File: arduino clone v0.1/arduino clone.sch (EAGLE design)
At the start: 18 parts, among them U101 ATMEGA328P_TQFP, U201 CH340G

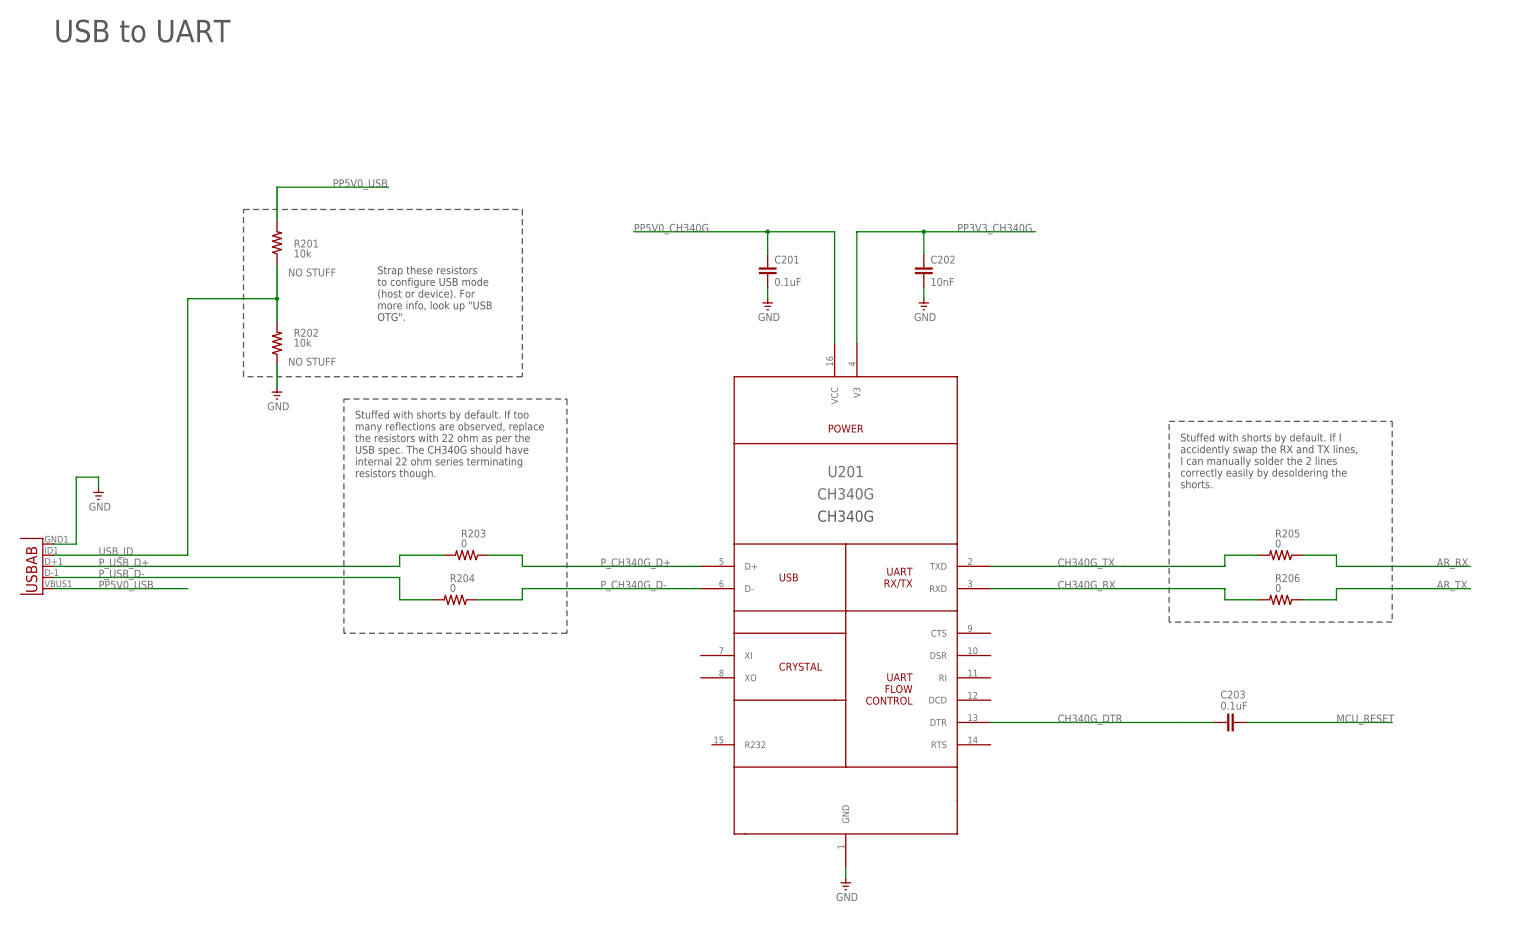
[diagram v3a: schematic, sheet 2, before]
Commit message: disconnect USB nets from connector
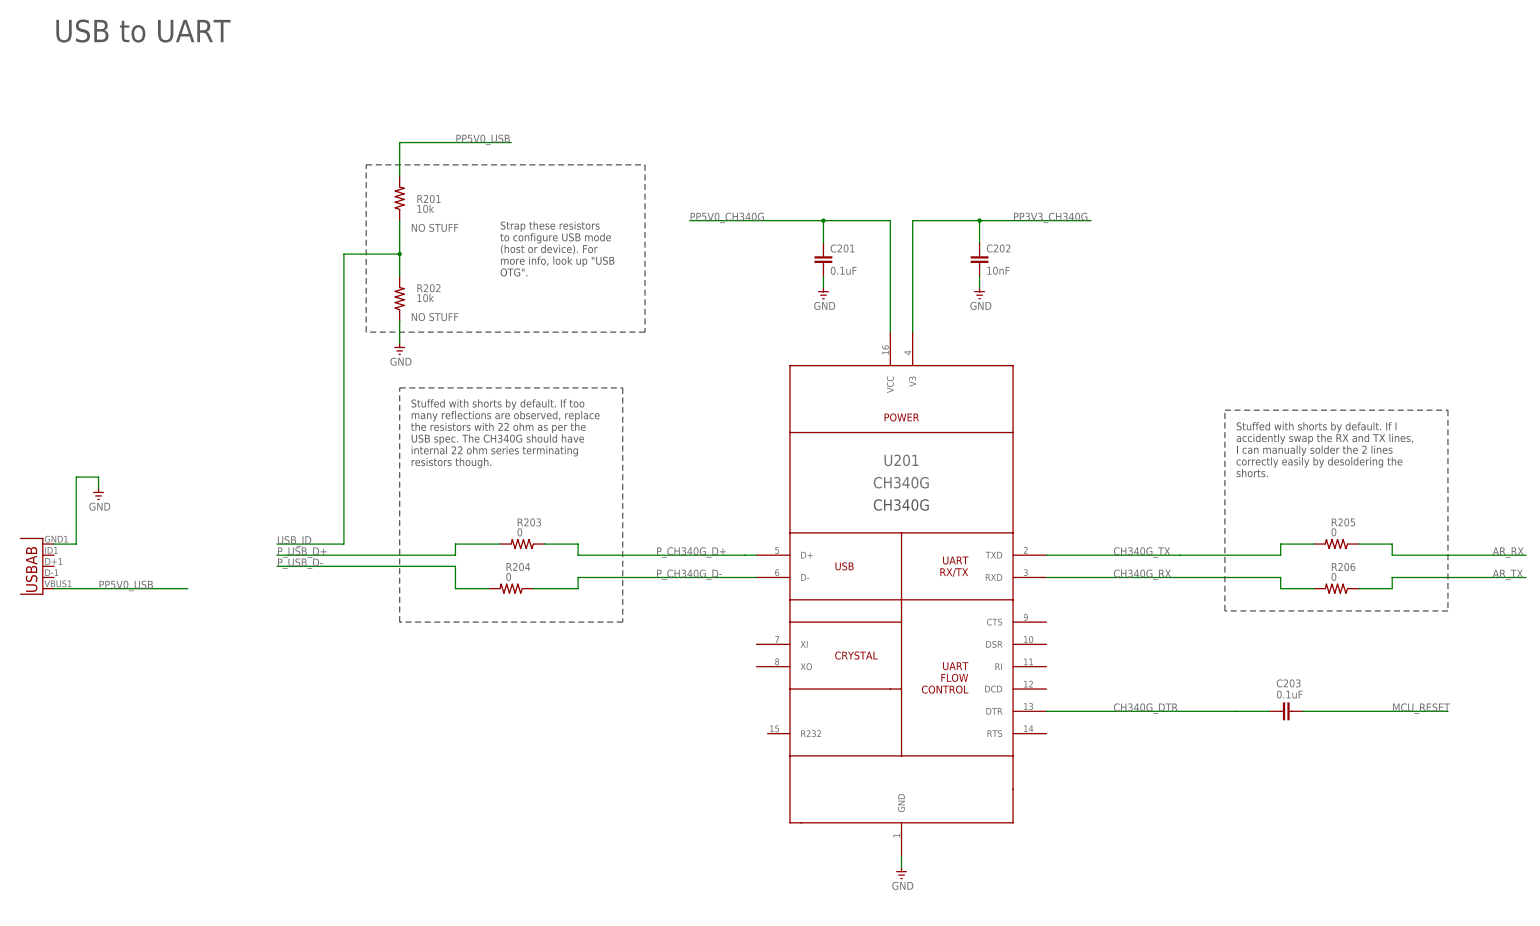
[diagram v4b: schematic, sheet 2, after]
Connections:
- net P_USB_D+: no longer J1.D+
- net P_USB_D-: no longer J1.D-
- net USB_ID: no longer J1.USBID
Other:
- moved on the sheet: C201, C202, C203, R201, R202, R203, R204, R205, R206, U201

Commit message: add signal nets to USB connector
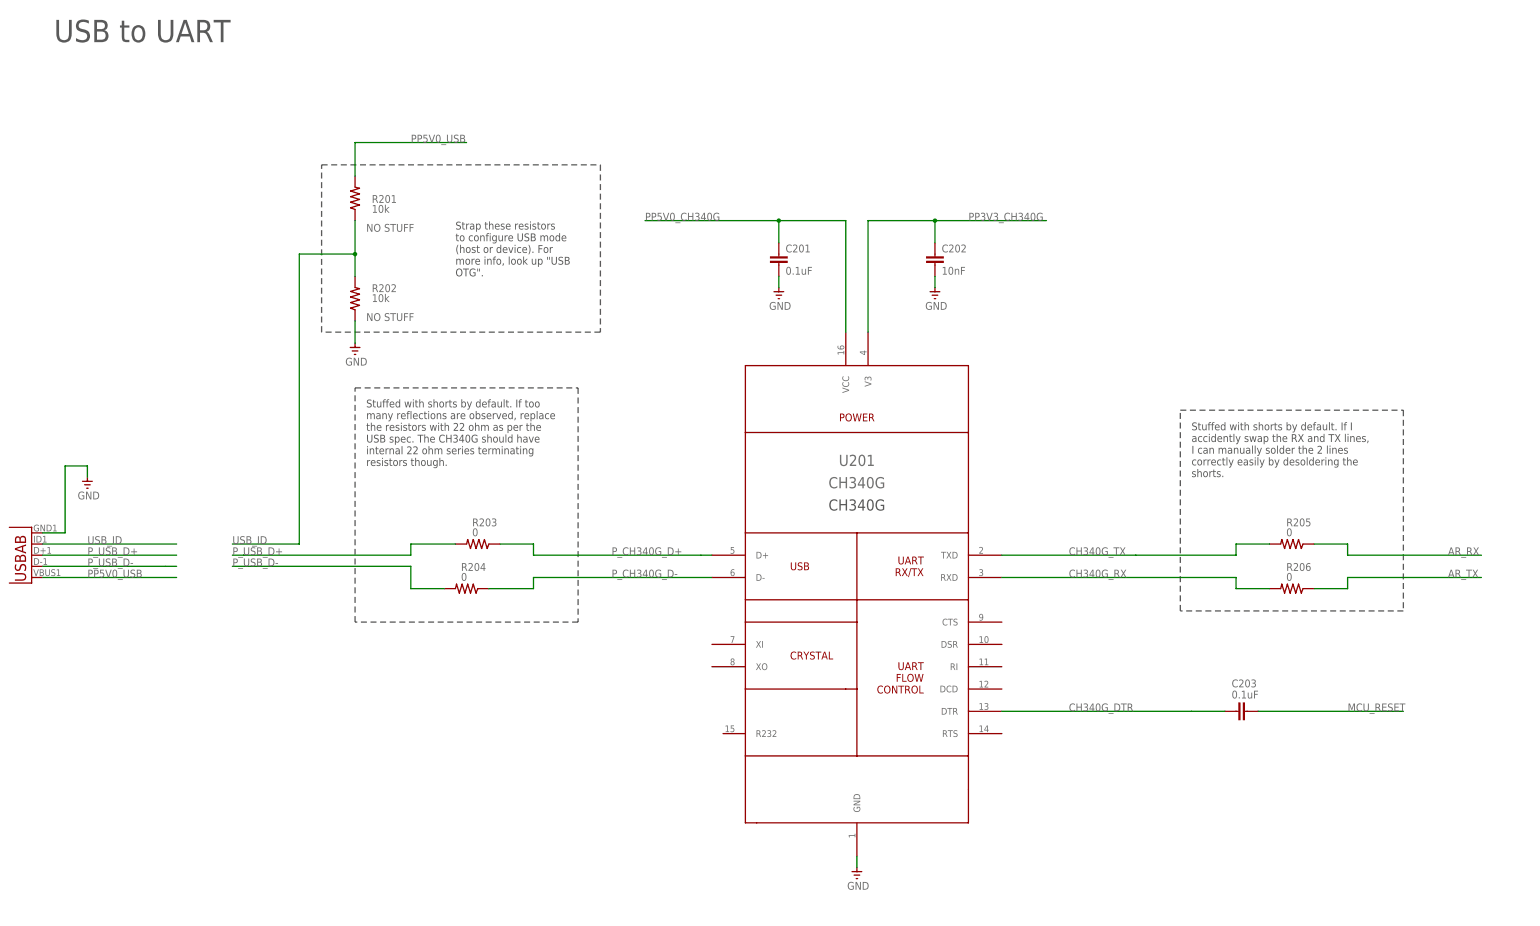
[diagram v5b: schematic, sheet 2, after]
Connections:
- net P_USB_D+: now also J1.D+
- net P_USB_D-: now also J1.D-
- net USB_ID: now also J1.USBID
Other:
- moved on the sheet: C201, C202, C203, R201, R202, R203, R204, R205, R206, U201

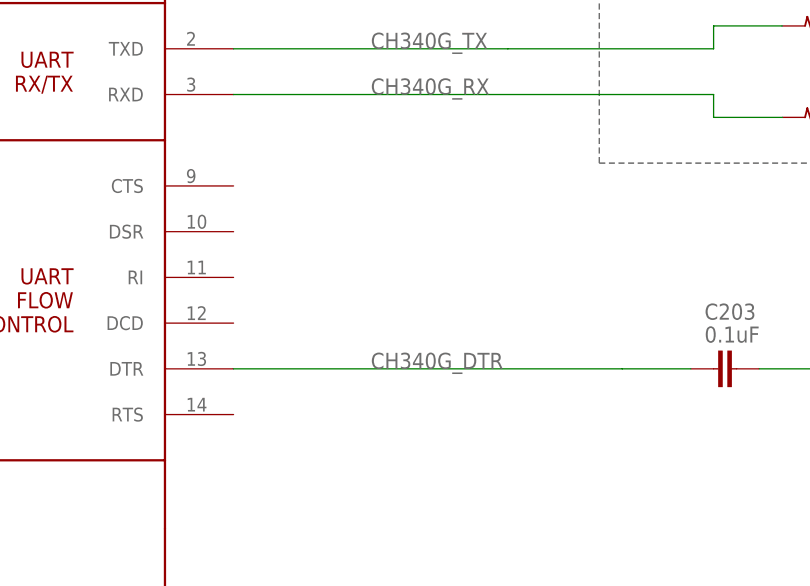
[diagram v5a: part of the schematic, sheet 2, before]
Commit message: add named nets for CH350G UART flow control
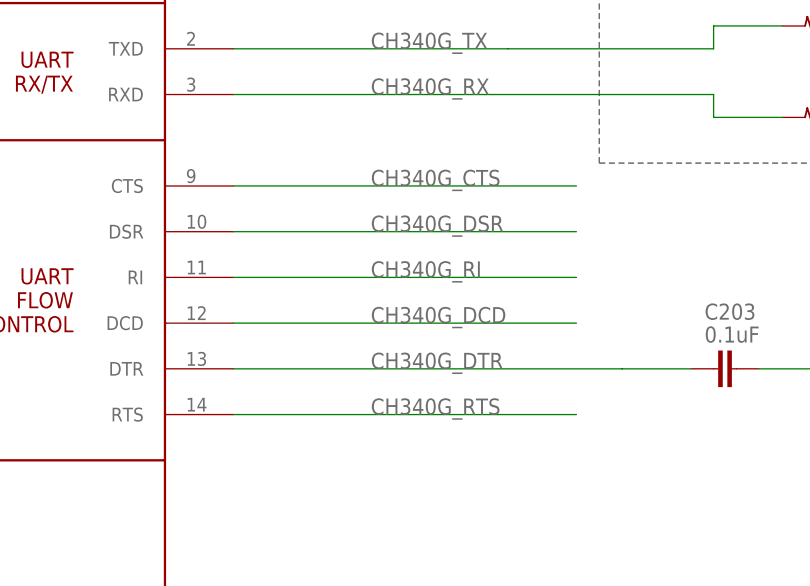
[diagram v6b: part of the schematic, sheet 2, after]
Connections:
- new net CH340G_CTS: U201.CTS
- new net CH340G_DCD: U201.DCD
- new net CH340G_DSR: U201.DSR
- new net CH340G_RI: U201.RI
- new net CH340G_RTS: U201.RTS
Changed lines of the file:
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@@
+</segment>
+</net>
+<net name="CH340G_CTS" class="0">
+<segment>
+<pinref part="U201" gate="G$1" pin="CTS"/>
+<wire x1="241.3" y1="106.68" x2="279.4" y2="106.68" width="0.1524" layer="91"/>
+<label x="256.54" y="106.68" size="1.778" layer="95"/>
+</segment>
+</net>
+<net name="CH340G_DSR" class="0">
+<segment>
+<pinref part="U201" gate="G$1" pin="DSR"/>
+<wire x1="241.3" y1="101.6" x2="279.4" y2="101.6" width="0.1524" layer="91"/>
+<label x="256.54" y="101.6" size="1.778" layer="95"/>
+</segment>
+</net>
+<net name="CH340G_RI" class="0">
+<segment>
+<pinref part="U201" gate="G$1" pin="RI"/>
+<wire x1="241.3" y1="96.52" x2="279.4" y2="96.52" width="0.1524" layer="91"/>
+<label x="256.54" y="96.52" size="1.778" layer="95"/>
+</segment>
+</net>
+<net name="CH340G_DCD" class="0">
+<segment>
+<pinref part="U201" gate="G$1" pin="DCD"/>
+<wire x1="241.3" y1="91.44" x2="279.4" y2="91.44" width="0.1524" layer="91"/>
+<label x="256.54" y="91.44" size="1.778" layer="95"/>
+</segment>
+</net>
+<net name="CH340G_RTS" class="0">
+<segment>
+<pinref part="U201" gate="G$1" pin="RTS"/>
+<wire x1="241.3" y1="81.28" x2="279.4" y2="81.28" width="0.1524" layer="91"/>
+<label x="256.54" y="81.28" size="1.778" layer="95"/>
 </segment>
 </net>

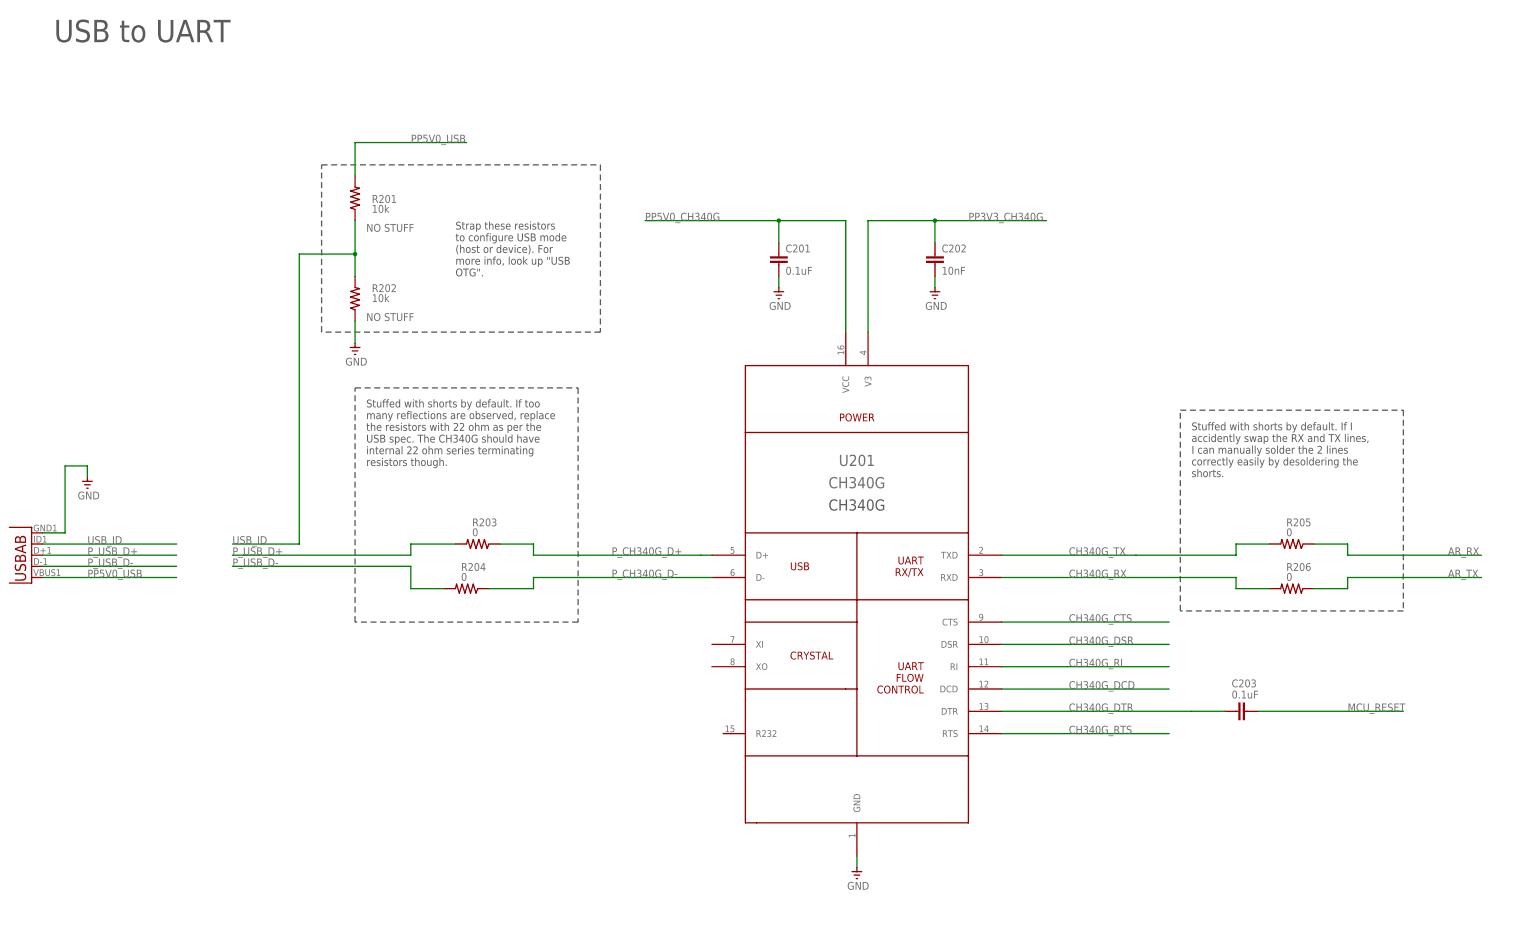
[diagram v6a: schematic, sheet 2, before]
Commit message: add FTDI breakout header
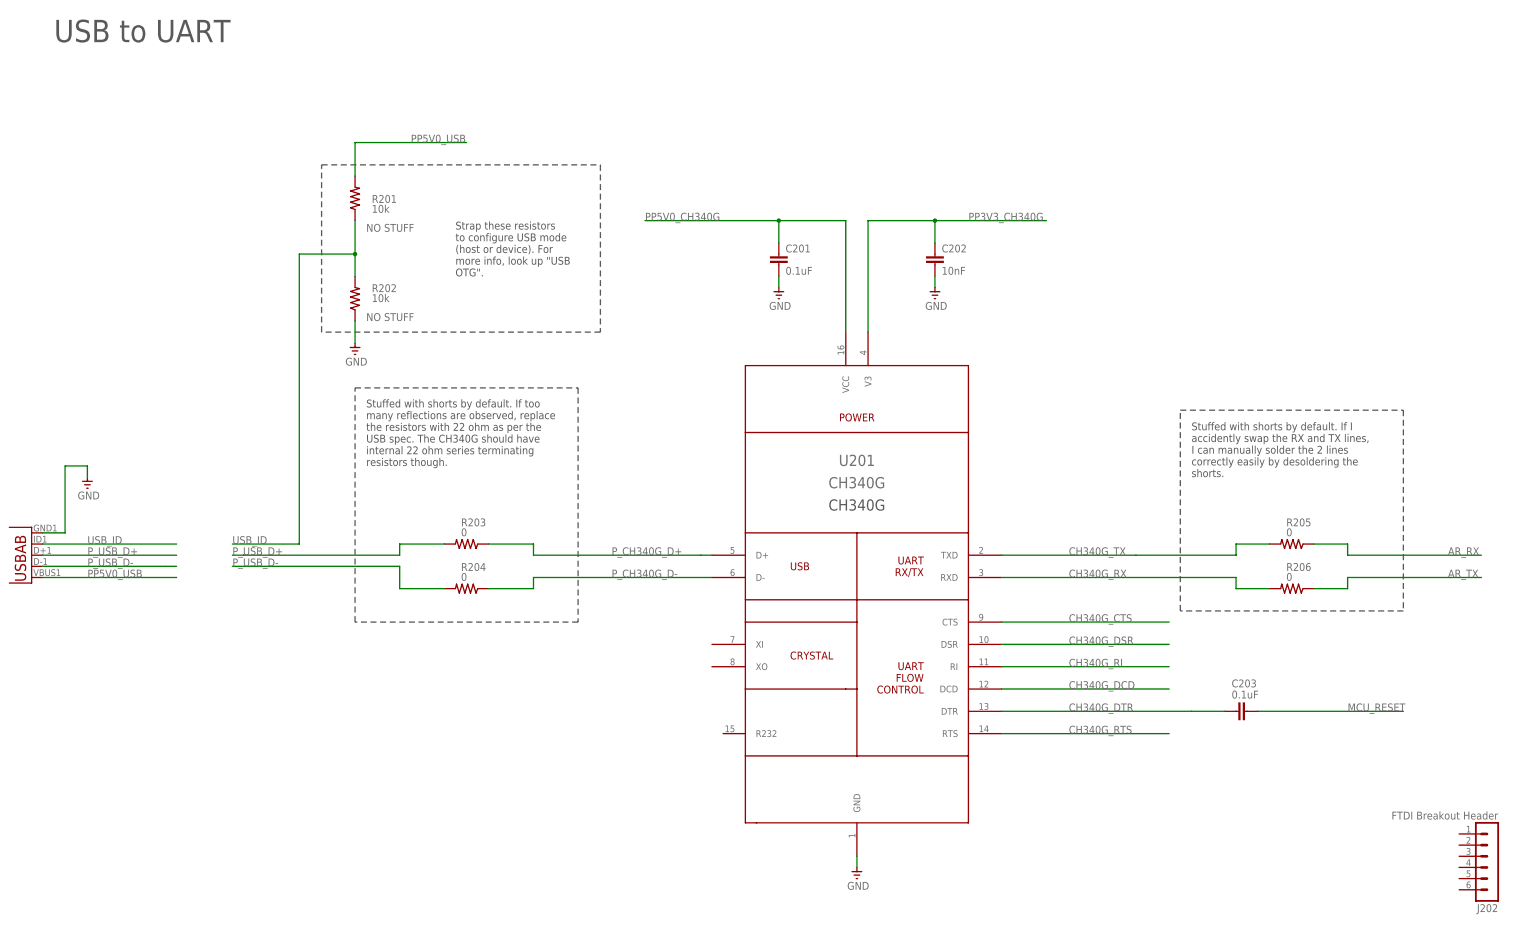
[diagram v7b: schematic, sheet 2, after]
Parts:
- added J202: FTDI Breakout Header, con-lstb:MA06-1
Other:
- moved on the sheet: R203
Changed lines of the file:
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@@
 <part name="R206" library="adafruit" deviceset="R-US_" device="R0805" value="0"/>
 <part name="C203" library="rcl" library_urn="urn:adsk.eagle:library:334" deviceset="C-EU" device="C0805" package3d_urn="urn:adsk.eagle:package:23617/2" value="0.1uF"/>
+<part name="J202" library="con-lstb" library_urn="urn:adsk.eagle:library:162" deviceset="MA06-1" device="" package3d_urn="urn:adsk.eagle:package:8340/1" value="FTDI Breakout Header"/>
 </parts>
 <sheets>
@@
 <attribute name="VALUE" x="91.7575" y="165.1" size="1.778" layer="96"/>
 </instance>
-<instance part="R203" gate="G$1" x="121.92" y="124.46" smashed="yes" rot="R180">
-<attribute name="NAME" x="120.65" y="128.4986" size="1.778" layer="95"/>
-<attribute name="VALUE" x="120.65" y="126.238" size="1.778" layer="96"/>
+<instance part="R203" gate="G$1" x="119.38" y="124.46" smashed="yes" rot="R180">
+<attribute name="NAME" x="118.11" y="128.4986" size="1.778" layer="95"/>
+<attribute name="VALUE" x="118.11" y="126.238" size="1.778" layer="96"/>
 </instance>
 <instance part="R204" gate="G$1" x="119.38" y="114.3" smashed="yes" rot="R180">
@@
 <attribute name="VALUE" x="293.624" y="89.281" size="1.778" layer="96"/>
 </instance>
+<instance part="J202" gate="1" x="353.06" y="50.8" rot="R180"/>
 </instances>
 <busses>
@@
 <net name="P_USB_D-" class="0">
 <segment>
-<wire x1="66.04" y1="119.38" x2="106.68" y2="119.38" width="0.1524" layer="91"/>
-<wire x1="106.68" y1="119.38" x2="106.68" y2="114.3" width="0.1524" layer="91"/>
+<wire x1="66.04" y1="119.38" x2="104.14" y2="119.38" width="0.1524" layer="91"/>
+<wire x1="104.14" y1="119.38" x2="104.14" y2="114.3" width="0.1524" layer="91"/>
 <pinref part="R204" gate="G$1" pin="2"/>
-<wire x1="106.68" y1="114.3" x2="114.3" y2="114.3" width="0.1524" layer="91"/>
+<wire x1="104.14" y1="114.3" x2="114.3" y2="114.3" width="0.1524" layer="91"/>
 <label x="66.04" y="119.38" size="1.778" layer="95"/>
 </segment>
@@
 <wire x1="172.72" y1="121.92" x2="175.26" y2="121.92" width="0.1524" layer="91"/>
 <pinref part="R203" gate="G$1" pin="1"/>
-<wire x1="127" y1="124.46" x2="134.62" y2="124.46" width="0.1524" layer="91"/>
+<wire x1="124.46" y1="124.46" x2="134.62" y2="124.46" width="0.1524" layer="91"/>
 <wire x1="134.62" y1="124.46" x2="134.62" y2="121.92" width="0.1524" layer="91"/>
 <wire x1="134.62" y1="121.92" x2="172.72" y2="121.92" width="0.1524" layer="91"/>
@@
 <segment>
 <pinref part="R203" gate="G$1" pin="2"/>
-<wire x1="116.84" y1="124.46" x2="106.68" y2="124.46" width="0.1524" layer="91"/>
-<wire x1="106.68" y1="124.46" x2="106.68" y2="121.92" width="0.1524" layer="91"/>
+<wire x1="114.3" y1="124.46" x2="104.14" y2="124.46" width="0.1524" layer="91"/>
+<wire x1="104.14" y1="124.46" x2="104.14" y2="121.92" width="0.1524" layer="91"/>
 <label x="66.04" y="121.92" size="1.778" layer="95"/>
-<wire x1="106.68" y1="121.92" x2="68.58" y2="121.92" width="0.1524" layer="91"/>
+<wire x1="104.14" y1="121.92" x2="68.58" y2="121.92" width="0.1524" layer="91"/>
 <wire x1="68.58" y1="121.92" x2="66.04" y2="121.92" width="0.1524" layer="91"/>
 </segment>
